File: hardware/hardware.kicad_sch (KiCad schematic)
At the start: 30 parts, among them J2 AudioPlug4, SW1 SW_Push, SW2 SW_Push, SW3 SW_Push, SW4 SW_Push, SW5 SW_Push, SW6 SW_Push, SW7 SW_Push, U1 ProMicro

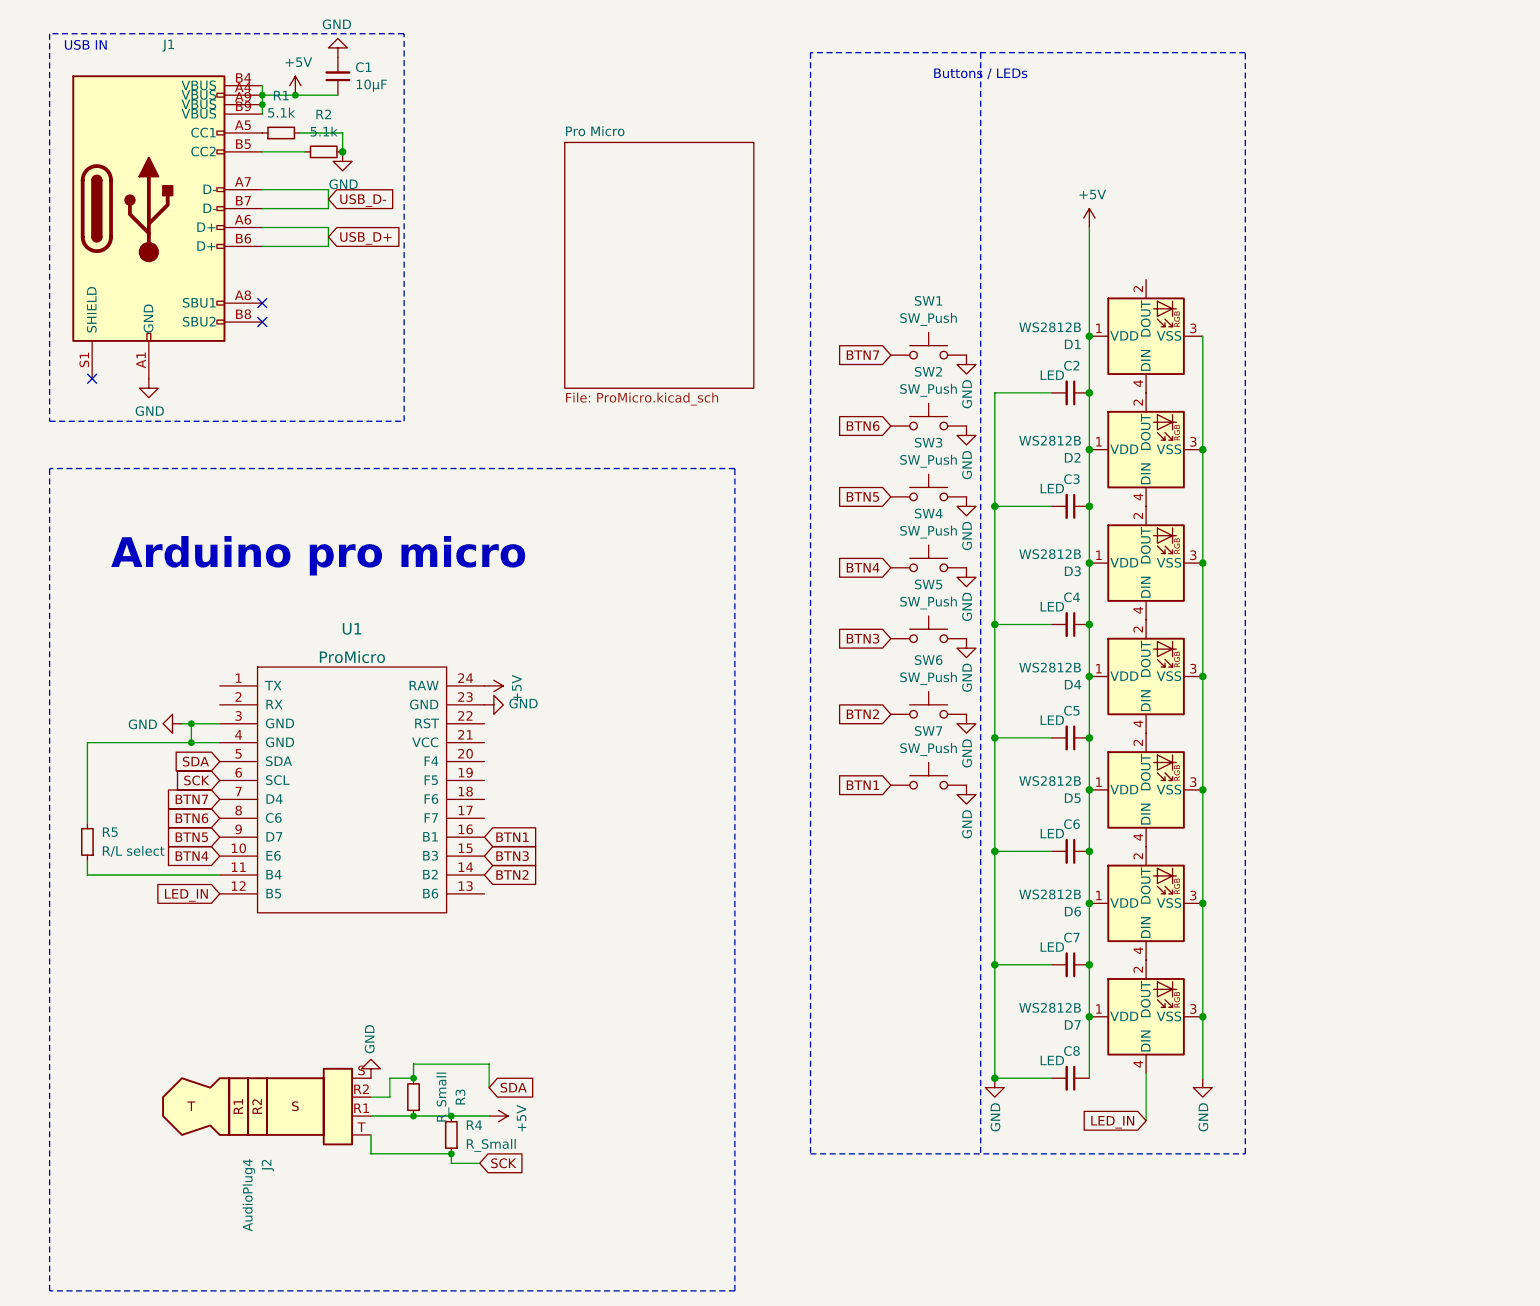
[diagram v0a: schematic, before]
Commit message: add backside and rounded corners
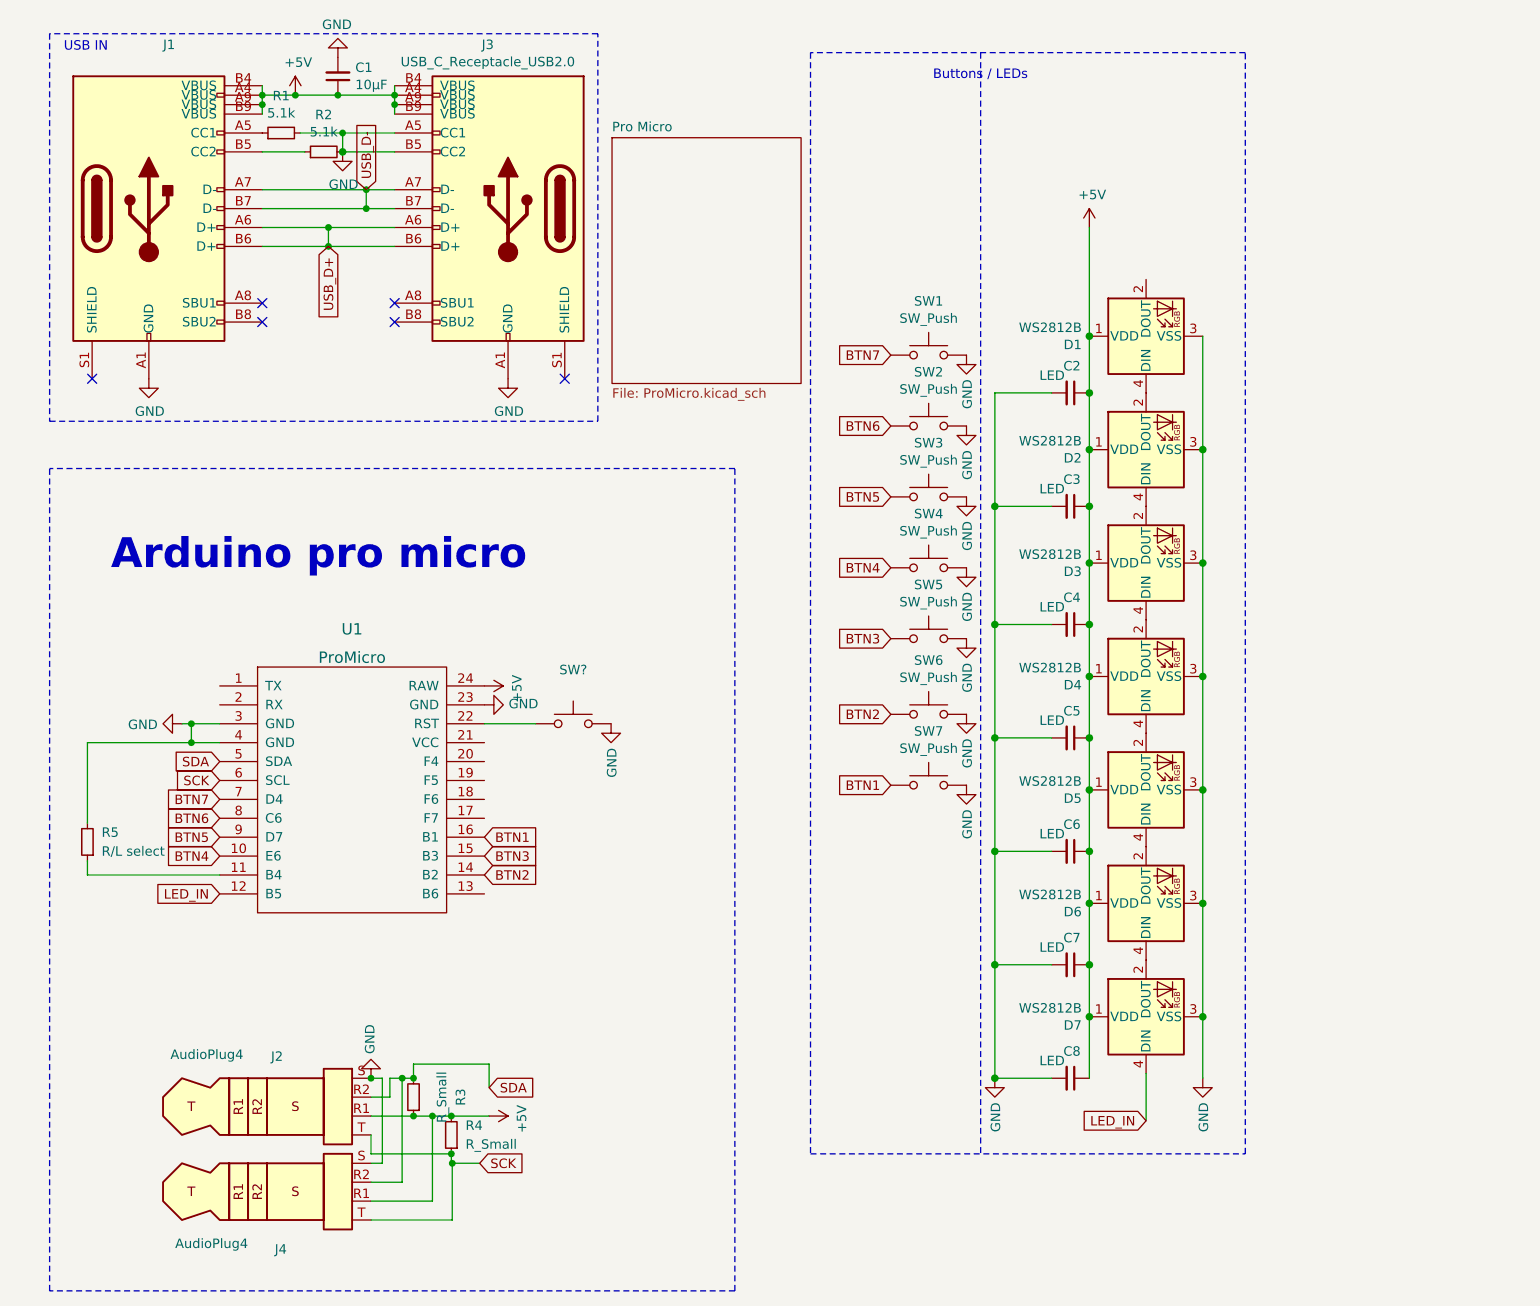
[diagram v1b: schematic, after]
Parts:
- added J3: USB_C_Receptacle_USB2.0, Library:SS52400002, symbol Library:USB_C_All_Receptacle_USB2.0
- added J4: AudioPlug4, Connector_Audio:Jack_3.5mm_PJ320D_Horizontal, symbol Connector:AudioPlug4
- added SW?: (no value), symbol Switch:SW_Push
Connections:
- net +5V: now also J3.A4 (VBUS), J3.A9 (VBUS), J3.B4 (VBUS), J3.B9 (VBUS), J4.R1
- net GND: now also J3.A1 (GND), J3.A12 (GND), J3.A5 (CC1), J3.B1 (GND), J3.B12 (GND), J3.B5 (CC2), J4.S, SW?.2
- net SCK: now also J4.T
- net SDA: now also J4.R2
- net USB_D+: now also J3.A6 (D+), J3.B6 (D+)
- net USB_D-: now also J3.A7 (D-), J3.B7 (D-)
- net at U1.22 (RST): now also SW?.1
- no-connect marks 3 -> 6

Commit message: start routing
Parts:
- removed R5: R/L select, Resistor_SMD:R_0805_2012Metric_Pad1.20x1.40mm_HandSolder, symbol Device:R_Small
- removed SW?: (no value), symbol Switch:SW_Push
- removed U1: ProMicro, Library:ProMicro, symbol promicro:ProMicro
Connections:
- net GND: now also R2.1; no longer J3.A5 (CC1), J3.B5 (CC2), R2.2
- net at J1.A5 (CC1): now also J3.A5 (CC1), R2.2; no longer R1.1
- net at J1.B5 (CC2): now also J3.B5 (CC2), R1.1; no longer R2.1
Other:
- moved on the sheet: R1, R2

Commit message: finish routing
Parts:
- added C18, C19, C20, C21, C22, C23, C24: LED, Capacitor_SMD:C_0603_1608Metric_Pad1.08x0.95mm_HandSolder, symbol Device:C_Small
- added D11, D12, D13, D14, D15, D16, D8: WS2812B, Library:LED_WS2812B_PLCC4_2.2x2.2mm, symbol LED:WS2812B
- added R12: (no value), symbol Device:R_Small
- added R13, R14, R15: 22, Resistor_SMD:R_0603_1608Metric_Pad0.98x0.95mm_HandSolder, symbol Device:R_Small
- added R17: 5.1k, Resistor_SMD:R_0603_1608Metric_Pad0.98x0.95mm_HandSolder, symbol Device:R_Small
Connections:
- net +5V: now also C18.1, C19.1, C20.1, C21.1, C22.1, C23.1, C24.1, D11.1 (VDD), D12.1 (VDD), D13.1 (VDD), D14.1 (VDD), D15.1 (VDD), D16.1 (VDD), D8.1 (VDD); no longer J1.B4 (VBUS), J1.B9 (VBUS), J3.B4 (VBUS), J3.B9 (VBUS)
- net GND: now also C18.2, C19.2, C20.2, C21.2, C22.2, C23.2, C24.2, D11.3 (VSS), D12.3 (VSS), D13.3 (VSS), D14.3 (VSS), D15.3 (VSS), D16.3 (VSS), D8.3 (VSS), R17.2
- net LED_IN: now also D16.4 (DIN)
- net USB_D+: now also R12.2, R13.2; no longer J1.A6 (D+), J1.B6 (D+), J3.A6 (D+), J3.B6 (D+)
- net USB_D-: now also R14.2, R15.2; no longer J1.A7 (D-), J1.B7 (D-), J3.A7 (D-), J3.B7 (D-)
- net at J1.B5 (CC2), R1.1: now also J3.B8 (SBU2); no longer J3.B5 (CC2)
- net at J1.B8 (SBU2): now also J3.B5 (CC2), R17.1
- net at D1.4 (DIN), D2.2 (DOUT): now also D11.2 (DOUT), D8.4 (DIN)
- net at D6.4 (DIN), D7.2 (DOUT): now also D15.4 (DIN), D16.2 (DOUT)
- net at D2.4 (DIN), D3.2 (DOUT): now also D11.4 (DIN), D12.2 (DOUT)
- net at D3.4 (DIN), D4.2 (DOUT): now also D12.4 (DIN), D13.2 (DOUT)
- net at D4.4 (DIN), D5.2 (DOUT): now also D13.4 (DIN), D14.2 (DOUT)
- net at D5.4 (DIN), D6.2 (DOUT): now also D14.4 (DIN), D15.2 (DOUT)
- new net: J1.A6 (D+), J1.B6 (D+), J3.A7 (D-), J3.B7 (D-), R12.1, R15.1
- new net: J1.A7 (D-), J1.B7 (D-), J3.A6 (D+), J3.B6 (D+), R13.1, R14.1
- no-connect marks 6 -> 4
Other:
- note added: "Bottom LEDs"
- moved on the sheet: J3
